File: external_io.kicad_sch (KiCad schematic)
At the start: 5 parts, among them J1 Conn_01x04_Socket, J2 Conn_01x02_Socket, J9 USB_C_Receptacle_USB2.0_16P

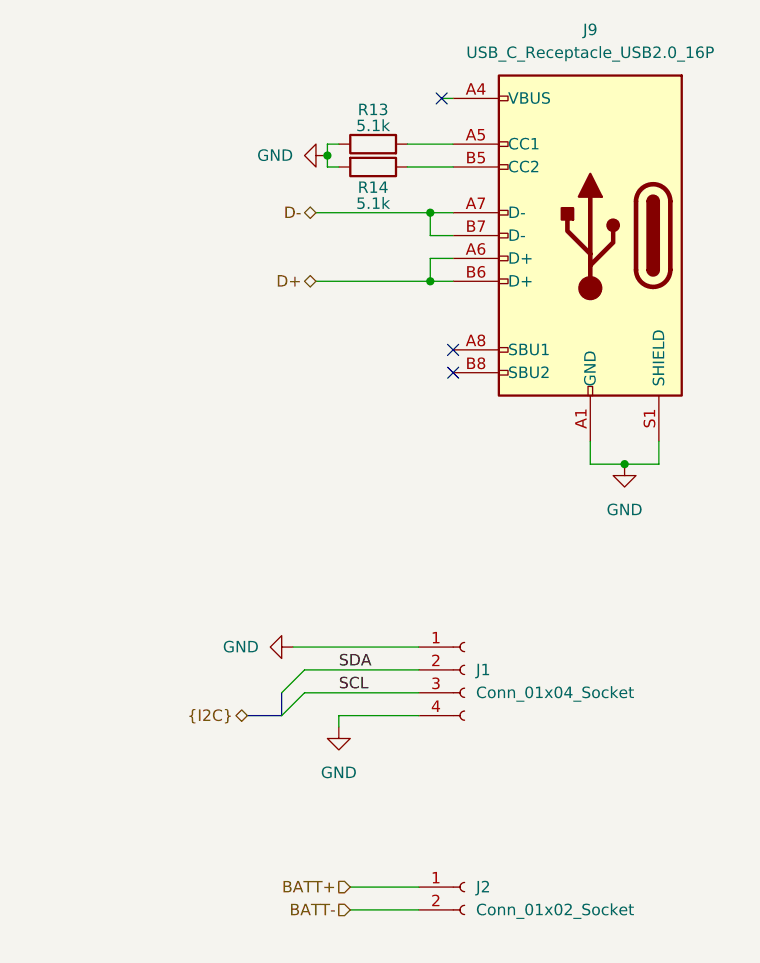
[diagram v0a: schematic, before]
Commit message: Updating schematic and adding in compnents to the PCB
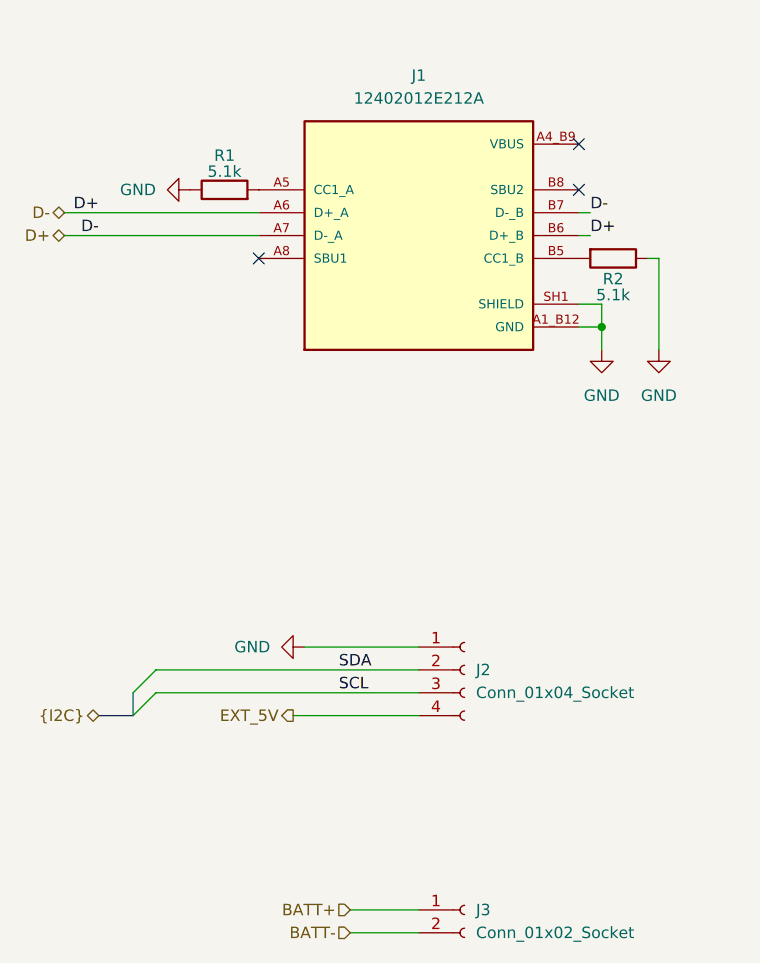
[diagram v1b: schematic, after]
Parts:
- removed J9: USB_C_Receptacle_USB2.0_16P, _BMS:AMPHENOL_12402012E212A, symbol Connector:USB_C_Receptacle_USB2.0_16P
- removed R13, R14: 5.1k, Resistor_SMD:R_0603_1608Metric, symbol Device:R
- added J1: 12402012E212A, 12402012E212A:AMPHENOL_12402012E212A, symbol _USB:12402012E212A
- added R1, R2: 5.1k, Resistor_SMD:R_0603_1608Metric, symbol Device:R
- renumbered J1 to J2, J2 to J3
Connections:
- net D+: now also J1.A6 (D+_A), J1.A7 (D-_A), J1.B6 (D+_B), J1.B7 (D-_B)
- net GND: now also J1.A1_B12 (GND), J1.B1_A12 (GND), J1.SH1 (SHIELD), J1.SH2 (SHIELD), J1.SH3 (SHIELD), J1.SH4 (SHIELD), R1.1, R2.1; no longer J2.4 (Pin_4)
- new net: J1.A5 (CC1_A), R1.2
- new net: J1.B5 (CC1_B), R2.2
- new net EXT_5V: J2.4 (Pin_4)
- new net VBUS: J1.A4_B9 (VBUS), J1.B4_A9 (VBUS)
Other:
- moved on the sheet: J3

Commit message: Layed on board. Still need to route
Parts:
- added U1, U2: USBLC6-2SC6, Package_TO_SOT_SMD:SOT-23-6, symbol Power_Protection:USBLC6-2SC6
- J1: footprint 12402012E212A:AMPHENOL_12402012E212A -> _BMS:AMPHENOL_12402012E212A
- J3: footprint (none) -> Connector_AMASS:AMASS_XT30PW-F_1x02_P2.50mm_Horizontal
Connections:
- net D+: now also U1.6 (I/O1); no longer J1.A6 (D+_A), J1.A7 (D-_A), J1.B7 (D-_B)
- net EXT_5V: now also U2.5 (VBUS)
- net GND: now also U1.2 (GND), U2.2 (GND)
- net SCL: now also U2.4 (I/O2); no longer J2.3 (Pin_3)
- net SDA: now also U2.6 (I/O1); no longer J2.2 (Pin_2)
- net BATT+ renamed PACK+
- net BATT- renamed PACK-
- new net: J1.A6 (D+_A), U1.1 (I/O1)
- new net: J1.A7 (D-_A), U1.3 (I/O2)
- new net: J2.2 (Pin_2), U2.1 (I/O1)
- new net: J2.3 (Pin_3), U2.3 (I/O2)
- new net D-: J1.B7 (D-_B), U1.4 (I/O2)
- no-connect marks 3 -> 4
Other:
- moved on the sheet: J2

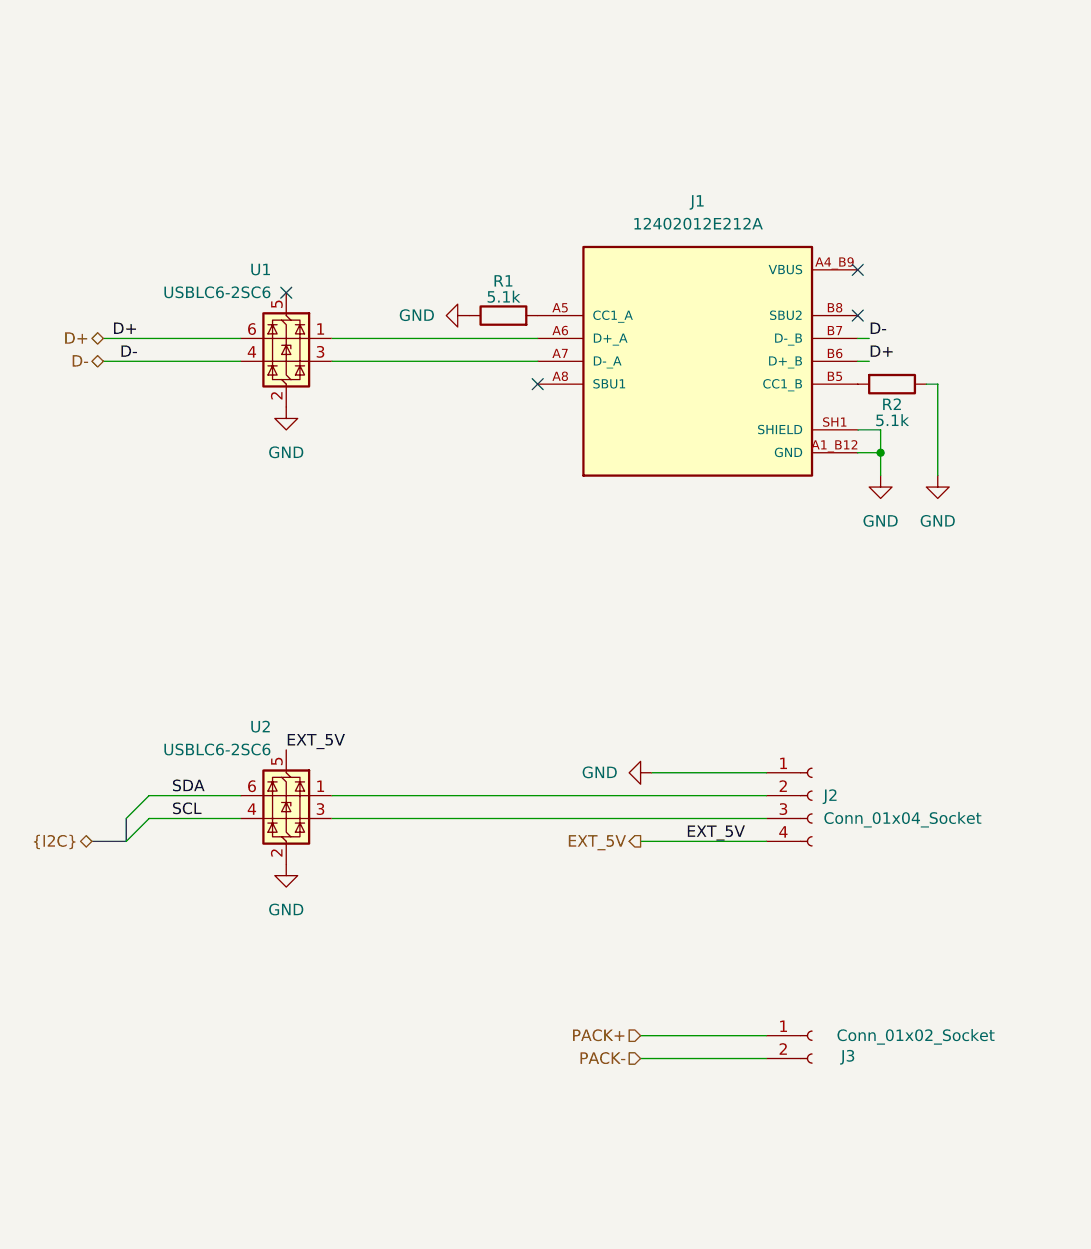
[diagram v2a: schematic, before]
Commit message: Adding proper grounding
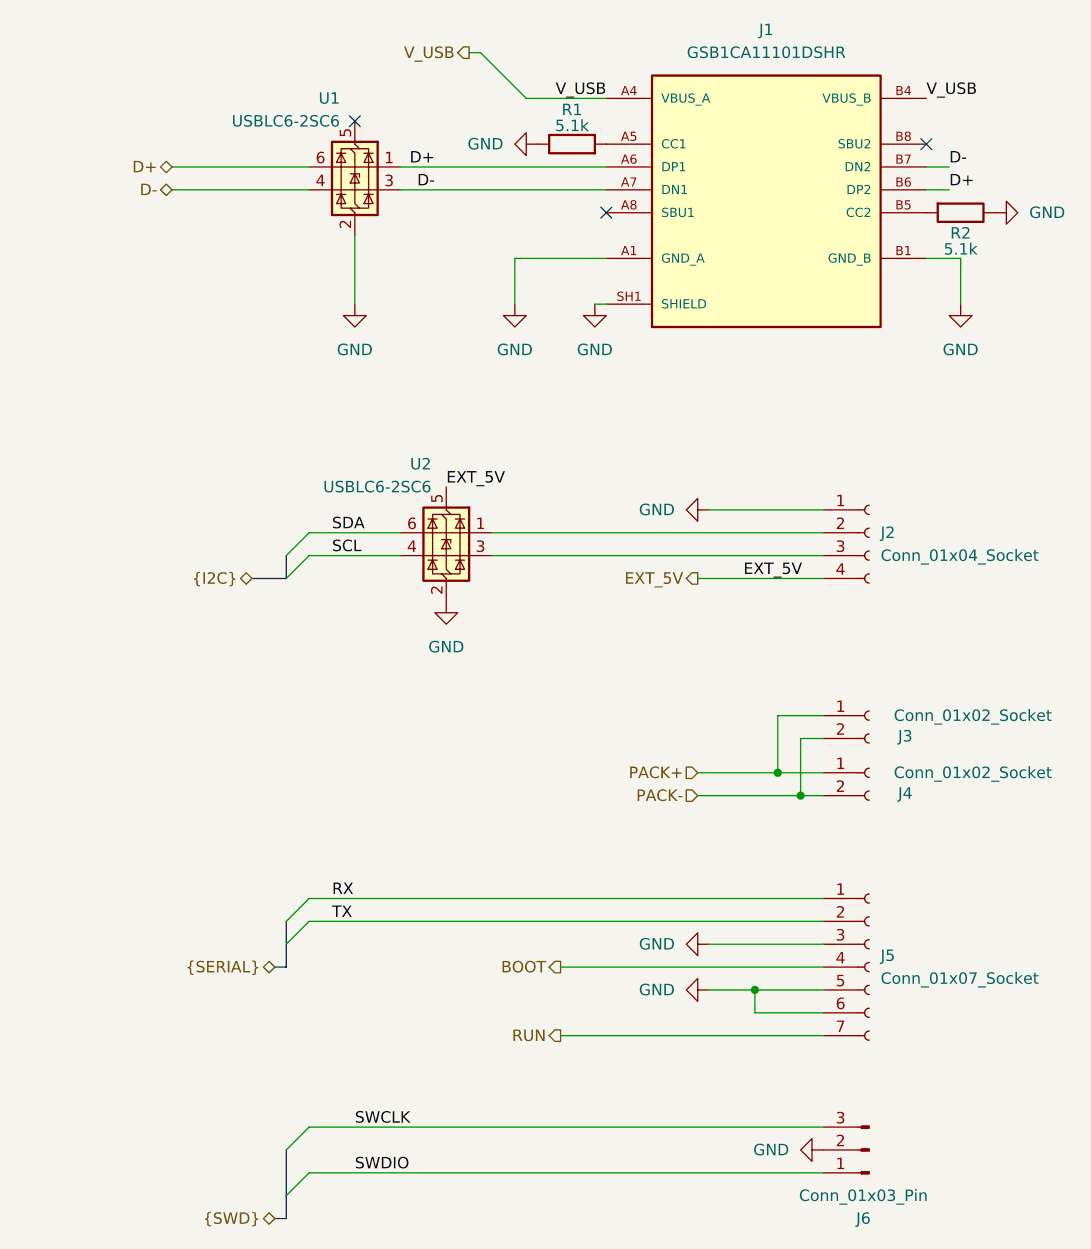
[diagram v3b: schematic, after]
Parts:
- removed J1: 12402012E212A, _BMS:AMPHENOL_12402012E212A, symbol _USB:12402012E212A
- added J1: GSB1CA11101DSHR, _BMS:AMPHENOL_GSB1CA11101DSHR, symbol _GSB1:GSB1CA11101DSHR
- added J3: Conn_01x02_Socket, Connector_AMASS:AMASS_XT30PW-F_1x02_P2.50mm_Horizontal, symbol Connector:Conn_01x02_Socket
- added J5: Conn_01x07_Socket, Connector_PinHeader_1.00mm:PinHeader_1x07_P1.00mm_Vertical, symbol Connector:Conn_01x07_Socket
- added J6: Conn_01x03_Pin, Connector_JST:JST_SH_SM03B-SRSS-TB_1x03-1MP_P1.00mm_Horizontal, symbol Connector:Conn_01x03_Pin
- J2: footprint (none) -> Connector_JST:JST_GH_SM04B-GHS-TB_1x04-1MP_P1.25mm_Horizontal; Mfr (none) -> JST Sales America Inc.; Mfr P/N (none) -> SM04B-GHS-TB; Supplier_1 (none) -> Digikey; Supplier_1 P/N (none) -> 455-1566-2-ND; Supplier_1 Price @ Qty (none) -> 1; Supplier_1 Unit Price (none) -> 0.38000
- renumbered J3 to J4
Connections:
- net D+: now also U1.1 (I/O1), J1.A6 (DP1), J1.B6 (DP2)
- net D-: now also U1.3 (I/O2), J1.A7 (DN1), J1.B7 (DN2)
- net GND: now also J1.A1 (GND_A), J1.A12 (GND_A), J1.B1 (GND_B), J1.B12 (GND_B), J1.SH1 (SHIELD), J1.SH2 (SHIELD), J1.SH3 (SHIELD), J1.SH4 (SHIELD), J5.3 (Pin_3), J5.5 (Pin_5), J5.6 (Pin_6), J6.2 (Pin_2)
- net PACK+: now also J3.1 (Pin_1)
- net PACK-: now also J3.2 (Pin_2)
- net at R1.2: now also J1.A5 (CC1)
- net at R2.2: now also J1.B5 (CC2)
- new net BOOT: J5.4 (Pin_4)
- new net RUN: J5.7 (Pin_7)
- new net RX: J5.1 (Pin_1)
- new net SWCLK: J6.3 (Pin_3)
- new net SWDIO: J6.1 (Pin_1)
- new net TX: J5.2 (Pin_2)
- new net VBUS_A: J1.A4 (VBUS_A), J1.A9 (VBUS_A), J1.B4 (VBUS_B), J1.B9 (VBUS_B)
- no-connect marks 4 -> 3
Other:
- moved on the sheet: J2, J4, R1, R2, U1, U2

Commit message: Lots of changfes
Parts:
- removed J1: GSB1CA11101DSHR, _BMS:AMPHENOL_GSB1CA11101DSHR, symbol _GSB1:GSB1CA11101DSHR
- added J6: 2169890001, _BMS:216989-0001_MOL, symbol _USBR:2169890001
- renumbered J2 to J1, J3 to J2, J4 to J3, J5 to J4, J6 to J5
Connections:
- net BOOT: now also J4.3 (Pin_3); no longer J4.4 (Pin_4)
- net D+: now also J6.A6 (DP1), J6.B6 (DP2)
- net D-: now also J6.A7 (DN1), J6.B7 (DN2)
- net GND: now also J4.4 (Pin_4), J6.A1 (GND), J6.A12 (GND), J6.B1 (GND), J6.B12 (GND); no longer J4.3 (Pin_3), J4.5 (Pin_5)
- net at R1.2: now also J6.A5 (CC1)
- net at R2.2: now also J6.B5 (CC2)
- new net NSHDN: J4.5 (Pin_5)
- new net V_USB: J6.A4 (VBUS), J6.A9 (VBUS), J6.B4 (VBUS), J6.B9 (VBUS)
- no-connect marks 3 -> 1
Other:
- moved on the sheet: J4, J5, R2

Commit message: Tweaks and production files
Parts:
- removed J6: 2169890001, _BMS:216989-0001_MOL, symbol _USBR:2169890001
- removed R2: 5.1k, Resistor_SMD:R_0603_1608Metric, symbol Device:R
- added J1: UJ20-C-H-G-SMT-1-P16-TR, _BMS:SAMESKY_UJ20-C-H-G-SMT-1-P16-TR, symbol _USBSKY:UJ20-C-H-G-SMT-1-P16-TR
- added R1: 5.1k, Resistor_SMD:R_0603_1608Metric, symbol Device:R
- renumbered J1 to J2, J2 to J3, J3 to J4, J4 to J5, J5 to J6, R1 to R2, U2 to U1, U1 to U2
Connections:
- net D+: now also J1.A6 (DP1), J1.B6 (DP2)
- net D-: now also J1.A7 (DN1), J1.B7 (DN2)
- net GND: now also J1.A1_B12 (GND), J1.B1_A12 (GND__1), J1.SH1 (SHIELD), J1.SH2 (SHIELD__1), J1.SH3 (SHIELD__2), J1.SH4 (SHIELD__3), R1.1
- net V_USB: now also J1.A4_B9 (VBUS), J1.B4_A9 (VBUS__1)
- net at R2.2: now also J1.A5 (CC1)
- new net: J1.B5 (CC2), R1.2
- no-connect marks 1 -> 3
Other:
- moved on the sheet: R2, U2

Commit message: Updating stuff
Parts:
- removed J5: Conn_01x07_Socket, Connector_PinHeader_1.00mm:PinHeader_1x07_P1.00mm_Vertical, symbol Connector:Conn_01x07_Socket
- removed J6: Conn_01x03_Pin, Connector_JST:JST_SH_SM03B-SRSS-TB_1x03-1MP_P1.00mm_Horizontal, symbol Connector:Conn_01x03_Pin
- added J10, J5, J6: Conn_01x03_Socket, Connector_PinHeader_2.54mm:PinHeader_1x03_P2.54mm_Vertical, symbol Connector:Conn_01x03_Socket
- R1, R2: Supplier_2 (none) -> JLCPCB; Supplier_2 P/N (none) -> C125891; Supplier_2 Price @ Qty (none) -> 1; Supplier_2 Unit Price (none) -> 0.0024
- U1, U2: Supplier_2 (none) -> JLCPCB; Supplier_2 P/N (none) -> C7519; Supplier_2 Price @ Qty (none) -> 1; Supplier_2 Unit Price (none) -> 0.1373
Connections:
- net D+: no longer J1.A6 (DP1), J1.B6 (DP2), U2.1 (I/O1)
- net D-: no longer J1.A7 (DN1), J1.B7 (DN2), U2.3 (I/O2)
- net GND: now also J10.3 (Pin_3), J5.2 (Pin_2)
- net RX: now also J10.1 (Pin_1)
- net SWCLK: now also J5.1 (Pin_1)
- net SWDIO: now also J5.3 (Pin_3)
- net TX: now also J10.2 (Pin_2)
- net V_USB: now also U2.5 (VBUS)
- new net Dn: J1.A7 (DN1), J1.B7 (DN2), U2.3 (I/O2)
- new net Dp: J1.A6 (DP1), J1.B6 (DP2), U2.1 (I/O1)
- no-connect marks 3 -> 2
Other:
- note added: "I2C"
- note added: "MISC SIGNALS"
- note added: "SERIAL"
- note added: "SWD"
- note added: "USBC"
- moved on the sheet: J1, J2, J3, J4, R1, U1

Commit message: Placement
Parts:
- added TP1, TP2, TP3: TestPoint, TestPoint:TestPoint_Keystone_5015_Micro_Mini, symbol Connector:TestPoint
- renumbered J3 to J2, J4 to J3, J2 to J4, J6 to J5, J10 to J6, J5 to J7, U2 to U1, U1 to U2
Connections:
- net GND: now also J5.2 (Pin_2)
- net BOOT: now reaches J5.1 (Pin_1)
- net RUN: now reaches J5.3 (Pin_3)
- new net WDT: TP2.1
- new net XALERT: TP1.1
- new net nSHDN: TP3.1

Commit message: Prelim placement done
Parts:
- removed J2: Conn_01x02_Socket, Connector_AMASS:AMASS_XT30PW-F_1x02_P2.50mm_Horizontal, symbol Connector:Conn_01x02_Socket
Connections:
- net PACK+: now also J3.2 (Pin_2); no longer J3.1 (Pin_1)
- net PACK-: now also J3.1 (Pin_1); no longer J3.2 (Pin_2)
